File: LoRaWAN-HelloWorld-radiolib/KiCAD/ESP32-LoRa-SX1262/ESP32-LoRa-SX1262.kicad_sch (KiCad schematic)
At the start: 2 parts, among them U1 ESP32-DEVKITC-32UE, U2 SX1262

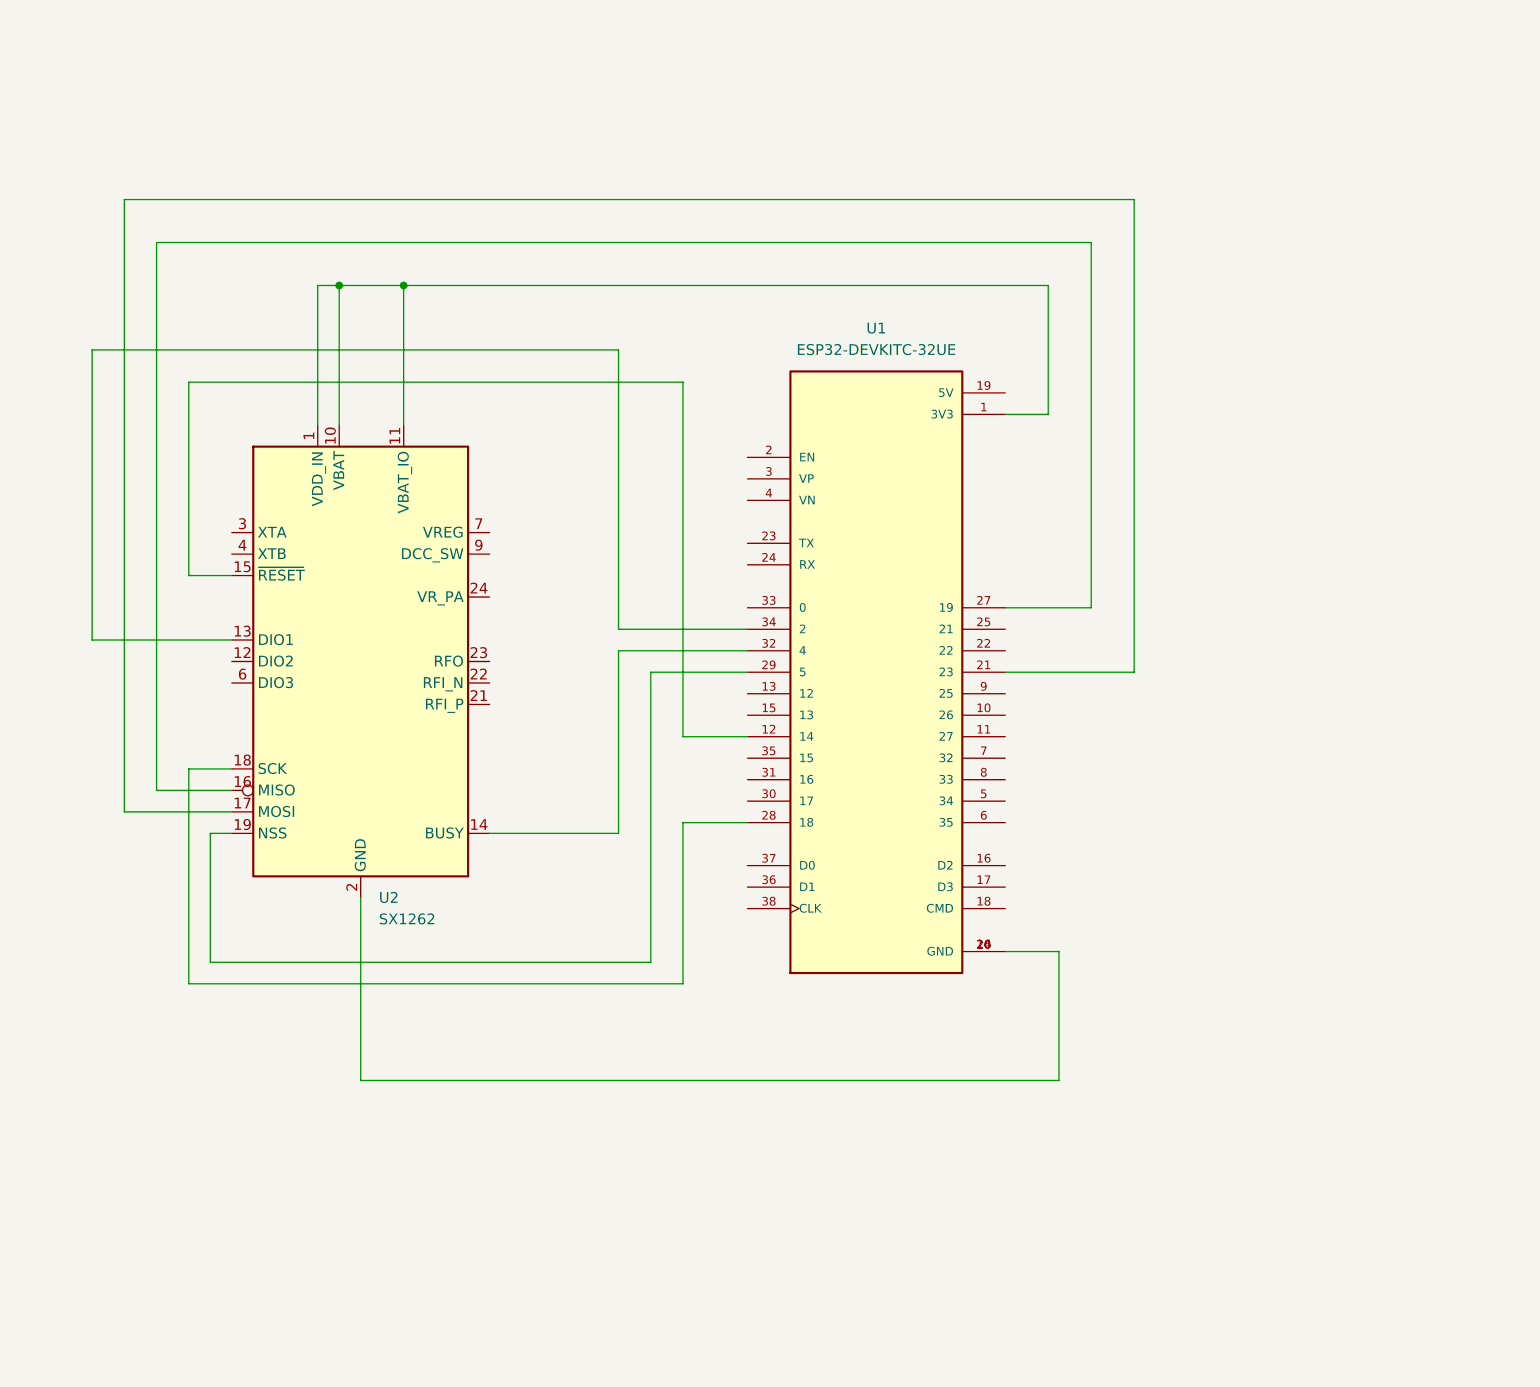
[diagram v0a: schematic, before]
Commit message: Roll back to full schema for SX1262 including all other sensors
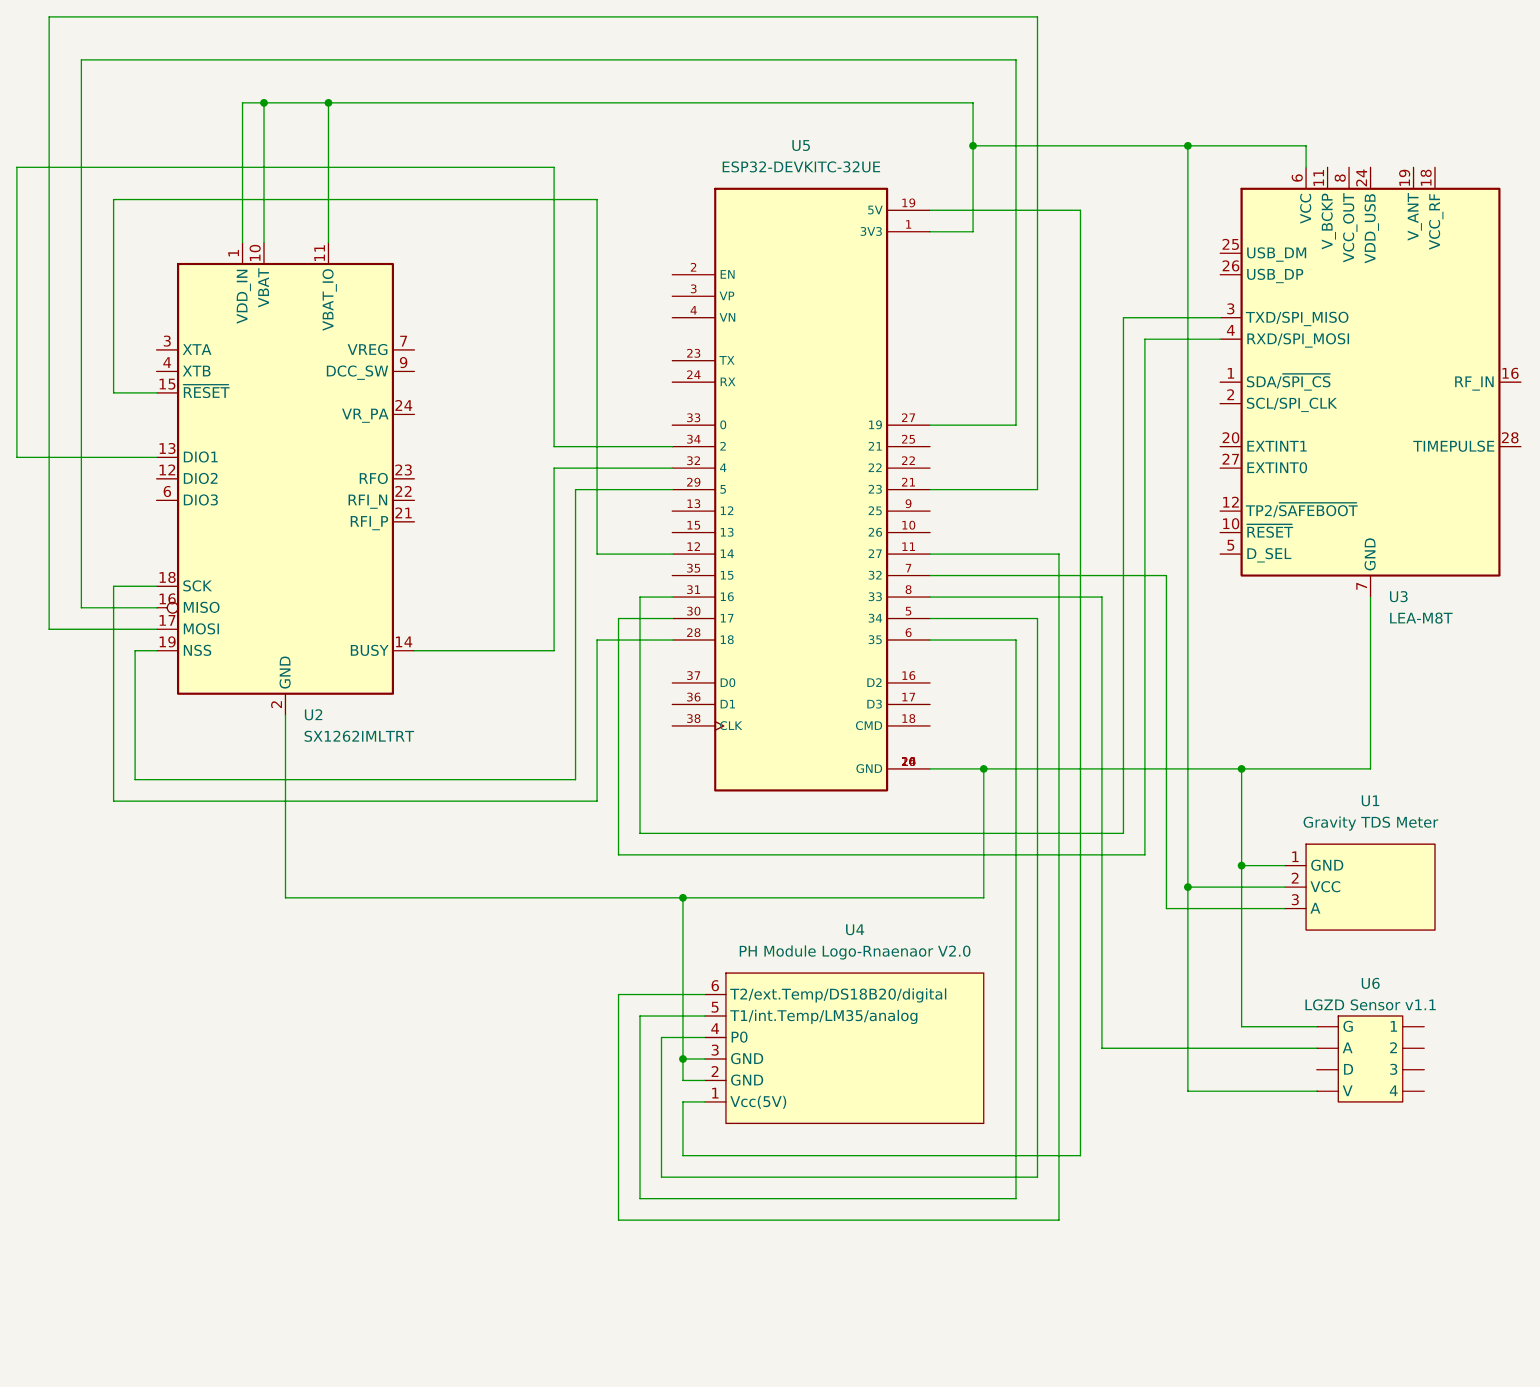
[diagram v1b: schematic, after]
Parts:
- removed U1: ESP32-DEVKITC-32UE, footprints:ESPRESSIF_ESP32-DEVKITC-32UE, symbol ESP32:ESP32-DEVKITC-32UE
- added U1: Gravity TDS Meter, symbol AdditionalFromVoc:Gravity_TDS_Meter_V1.0
- added U3: LEA-M8T, RF_GPS:ublox_LEA, symbol RF_GPS:LEA-M8T
- added U4: PH Module Logo-Rnaenaor V2.0, symbol AdditionalFromVoc:PH_Module_Logo-Rnaenaor
- added U5: ESP32-DEVKITC-32UE, symbol AdditionalFromVoc:ESP32-DEVKITC-32UE
- added U6: LGZD Sensor v1.1, symbol AdditionalFromVoc:LGZD Sensor v1.1
- U2: value SX1262 -> SX1262IMLTRT
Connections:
- net at U2.1 (VDD_IN), U2.10 (VBAT), U2.11 (VBAT_IO): now also U1.2 (VCC), U3.6 (VCC), U5.1 (3V3), U6. (4)
- net at U2.15 (~{RESET}): now also U5.12 (14)
- net at U2.2 (GND), U2.20 (GND), U2.25 (GND)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: now also U1.1 (GND), U3.13 (GND), U3.14 (GND), U3.15 (GND), U3.17 (GND), U3.7 (GND), U4.2 (GND), U4.3 (GND), U5.14 (GND), U5.20 (GND), U5.26 (GND), U6. (4)
- net at U2.17 (MOSI): now also U5.21 (23)
- net at U2.16 (MISO): now also U5.27 (19)
- net at U2.18 (SCK): now also U5.28 (18)
- net at U2.19 (NSS): now also U5.29 (5)
- net at U2.14 (BUSY): now also U5.32 (4)
- net at U2.13 (DIO1): now also U5.34 (2)
- new net: U5.8 (33), U6. (4)
- new net: U4.6 (T2/ext.Temp/DS18B20/digital), U5.11 (27)
- new net: U4.1 (Vcc(5V)), U5.19 (5V)
- new net: U3.4 (RXD/SPI_MOSI), U5.30 (17)
- new net: U3.3 (TXD/SPI_MISO), U5.31 (16)
- new net: U4.4 (P0), U5.5 (34)
- new net: U4.5 (T1/int.Temp/LM35/analog), U5.6 (35)
- new net: U1.3 (A), U5.7 (32)
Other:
- company: FH-Hagenberg -> FH Upper Austria / Campus Hagenberg / MTD / IM
- title: ESP32-WROOM-32 | SX1262 -> ESP32 NodeMCU | SX1262 + Sensors
- moved on the sheet: U2

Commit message: Update schematic
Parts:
- added R1, R4: 10k, symbol Device:R
- added R2, R5: 20k, symbol Device:R
- added R3: 4.7k, symbol Device:R
- added U7: DS18B20, Package_TO_SOT_THT:TO-92_Inline, symbol Sensor_Temperature:DS18B20
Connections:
- net at U6. (4): now also U5.8 (33)
- net at U1.1 (GND), U2.2 (GND), U2.20 (GND)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: now also R2.1, R5.1, U7.1 (GND)
- net at U5.11 (27): now also R4.1, R5.2; no longer U4.6 (T2/ext.Temp/DS18B20/digital)
- net at U4.1 (Vcc(5V)), U5.19 (5V): now also R3.2, U7.3 (V_{DD})
- net at U5.5 (34): now also R1.1, R2.2; no longer U4.4 (P0)
- new net: R3.1, R4.2, U4.6 (T2/ext.Temp/DS18B20/digital), U7.2 (DQ)
- new net: R1.2, U4.4 (P0)
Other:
- note added: "3.3"
- note added: "CLK"
- note added: "CS"
